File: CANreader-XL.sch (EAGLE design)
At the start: 100 parts, among them IC1 MCP2551, IC2 TJA1055T/3, IC3 BD9G101G, IC4 LM1117IMPX-3.3, IC6 STM32F107RBT, IC7 DP83848I, Q1 25MHz, SW1 SLEEP, SW2 TERM, U1 HC_05, X1 MINI-USB, X2 SWD, X3 GPIO, X4 UART, X5 CAN

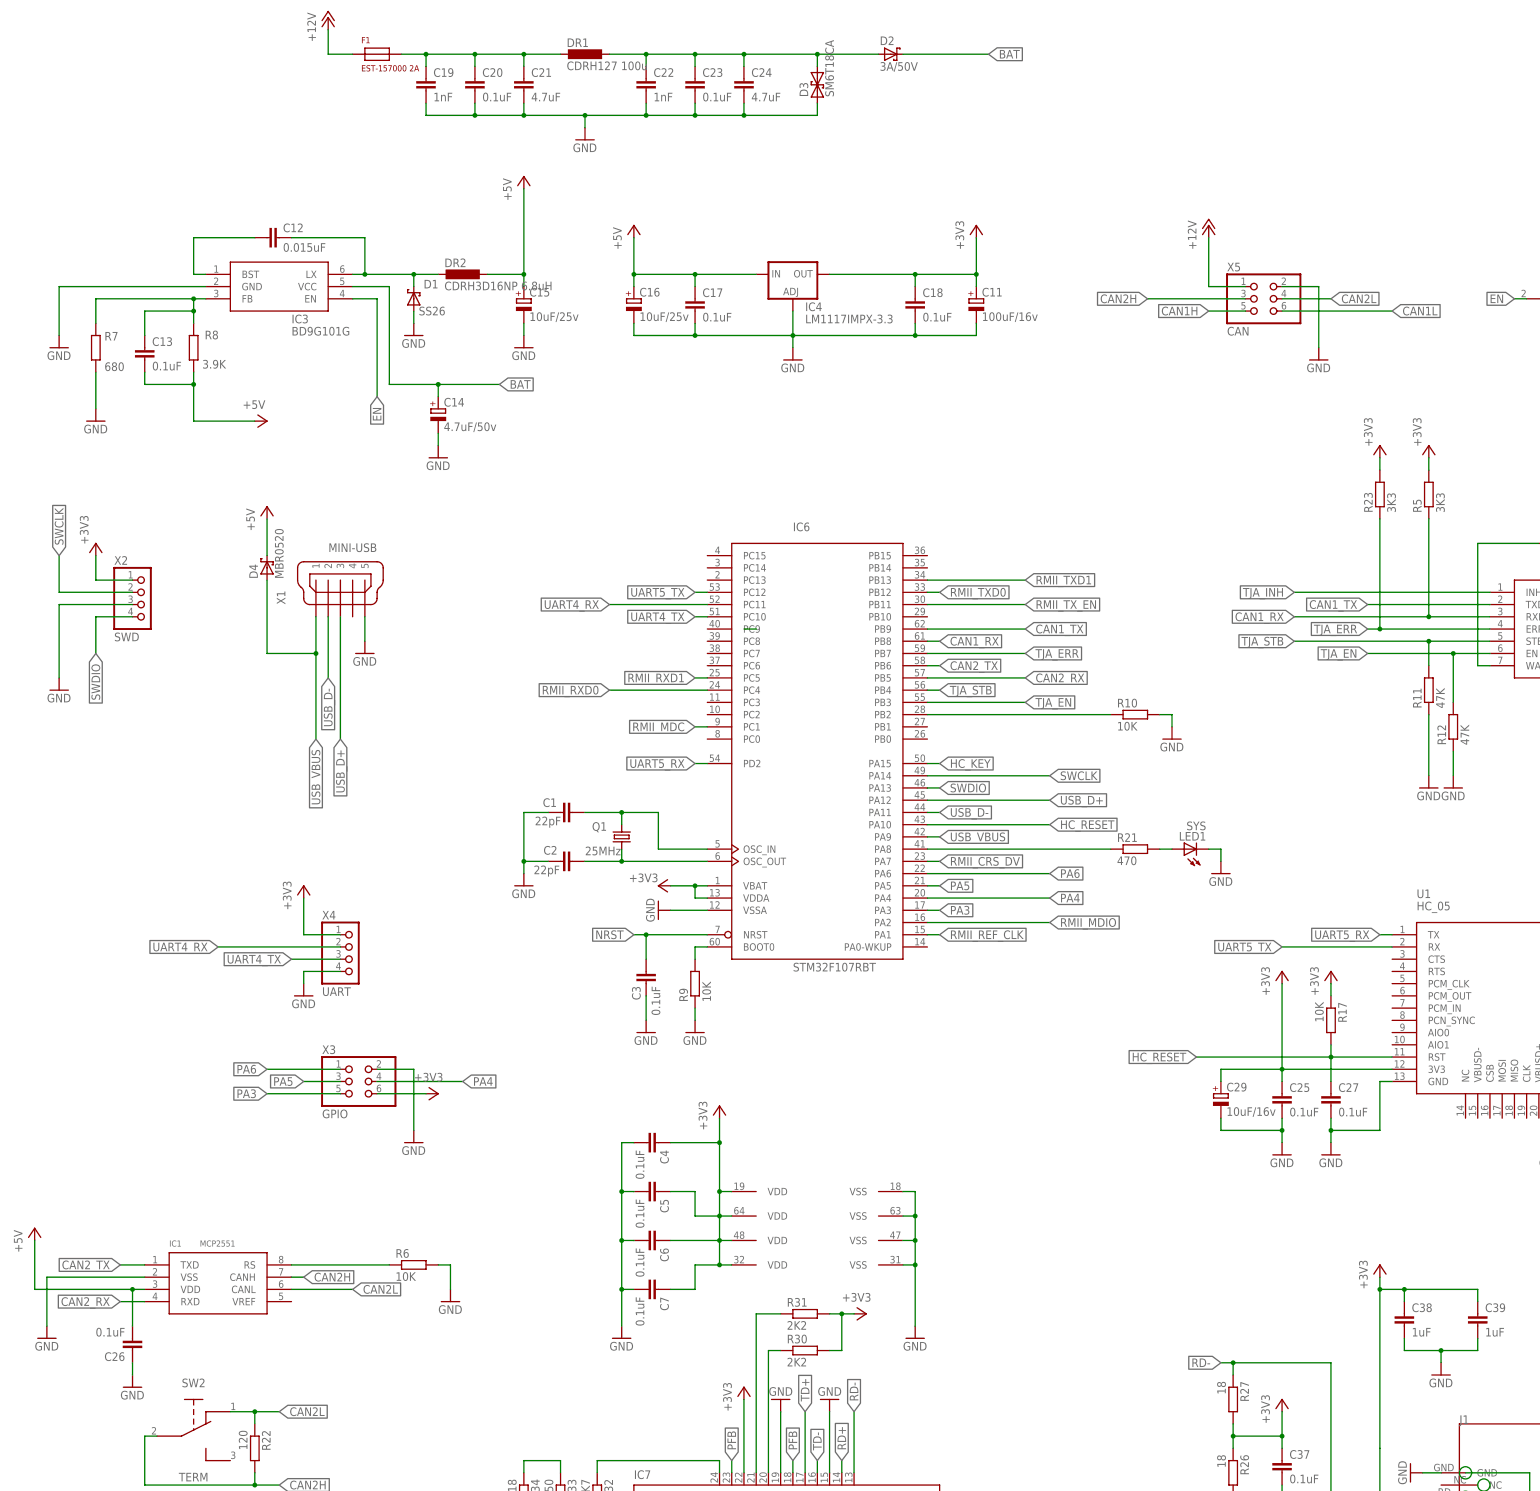
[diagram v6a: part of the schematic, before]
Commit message: MCP2562, usb connector
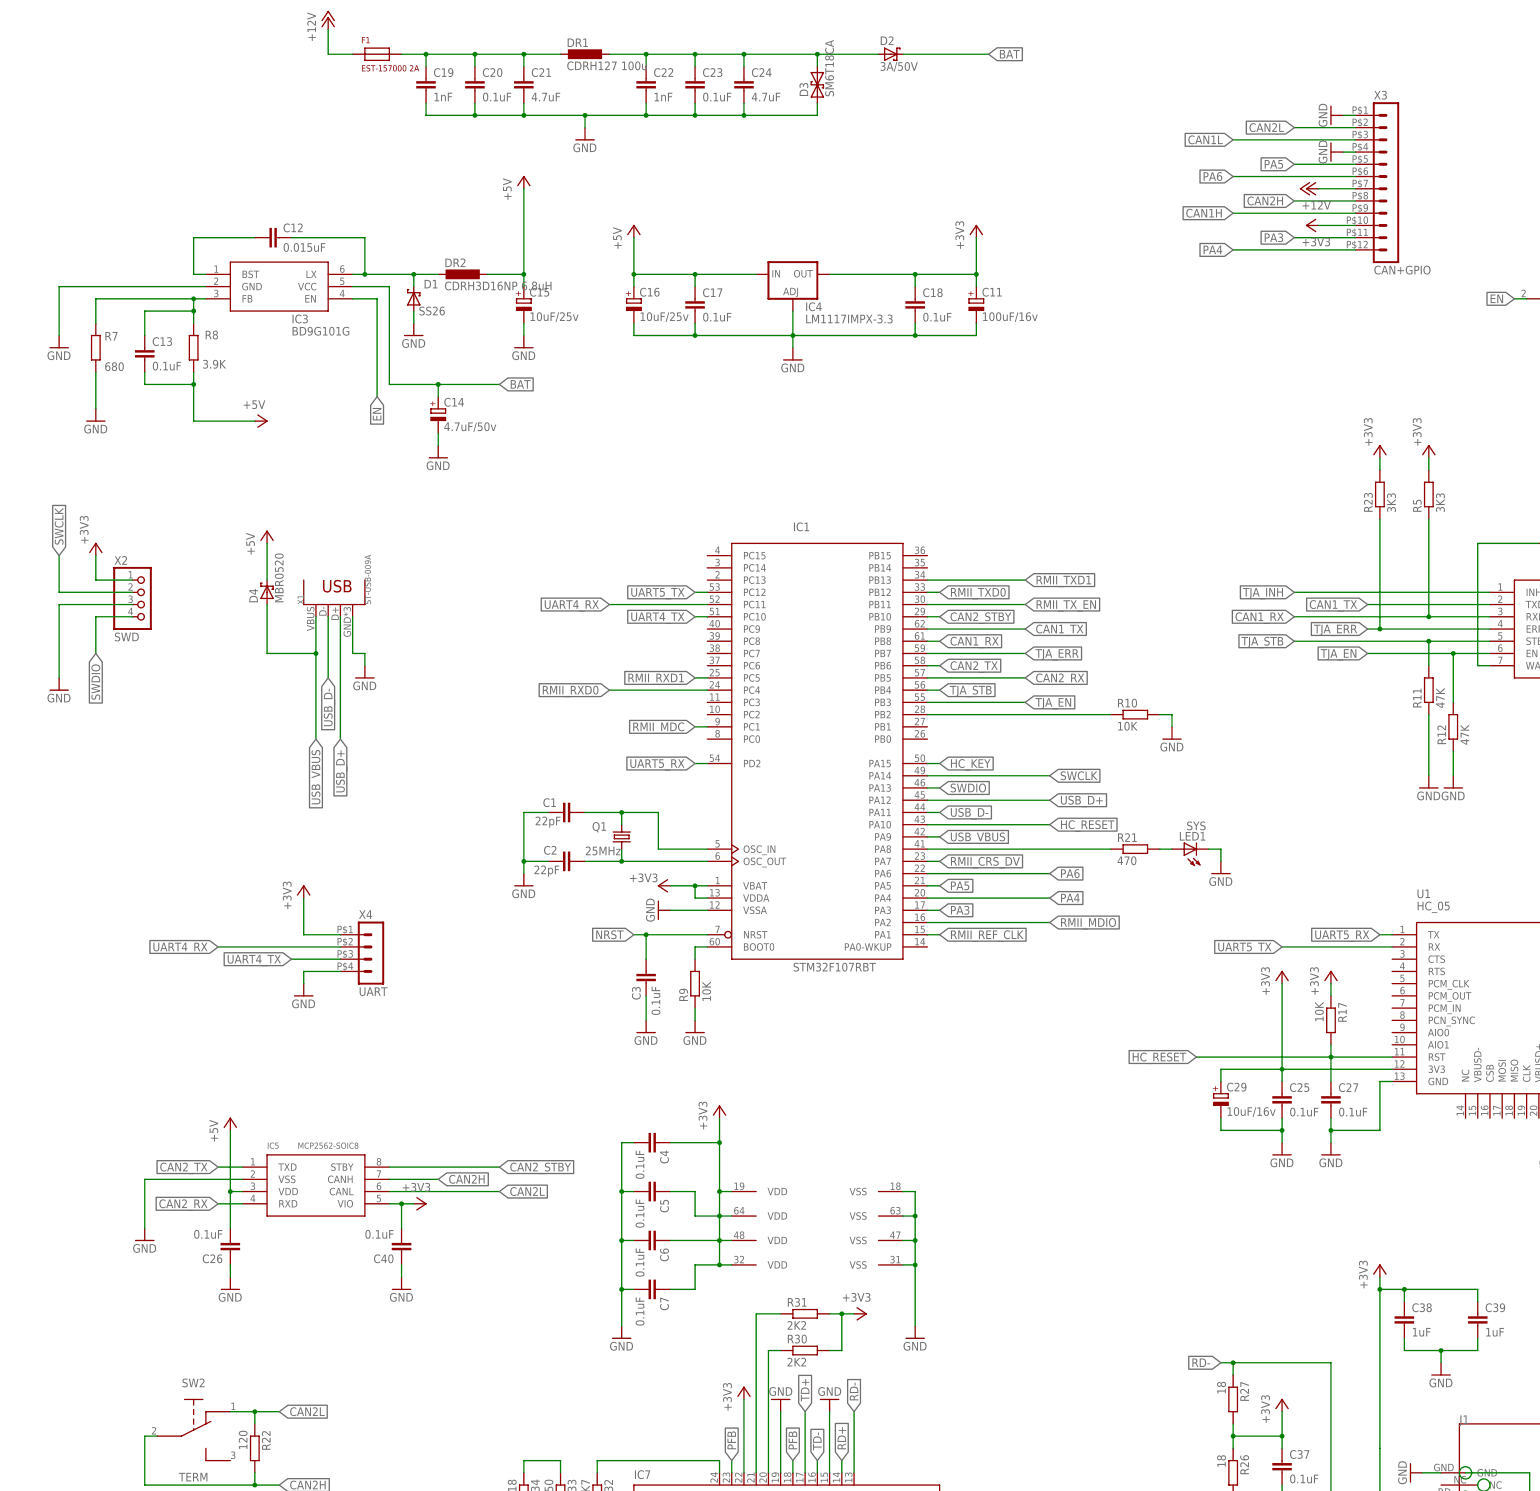
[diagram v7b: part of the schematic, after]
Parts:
- removed IC6: STM32F107RBT, micro-stm_v2:STM32F107RBT
- removed R6: 10K, rcl:R-EU_R0805
- removed X5: CAN, STM32_CAN-USB:PINHD-2X3/90
- added C40: 0.1uF, rcl:C-EUC0805
- added IC5: MCP2562-SOIC8, STM32_CAN-USB:MCP2562-SOIC8
- IC1: value MCP2551 -> STM32F107RBT; device STM32_CAN-USB:INTERFACE-MCP2551-I/SN(SOIC8) -> micro-stm_v2:STM32F107RBT
- X1: value MINI-USB -> ST-USB-009A; device STM32_CAN-USB:MINI-USB-UX60-MB-5ST -> Seeed-OPL-Connector:DIP-USB-B-TYPE-FMAL(4+2P-2.5-90D)
- X3: value GPIO -> CAN+GPIO; device STM32_CAN-USB:PINHD-2X3/90 -> con-molex-micro-fit-3_0:HEADER_POS12_43045-1200
- X4: device STM32_CAN-USB:PINHD-1X4/90 -> con-molex-micro-fit-3_0:HEADER_POS4_43045-0401
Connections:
- removed net N$5: IC1.RS, R6.1
- new net CAN2_STBY: IC1MCU.PB10, IC5.STBY
- net +12V: now also X3.7; no longer X5.1
- net +3V3: now also C40.2, IC1MCU.VBAT, IC1MCU.VDDA, IC1PWR.VDD@1, IC1PWR.VDD@2, IC1PWR.VDD@3, IC1PWR.VDD@4, IC5.VIO, X3.10; no longer IC6MCU.VBAT, IC6MCU.VDDA, IC6PWR.VDD@1, IC6PWR.VDD@2, IC6PWR.VDD@3, IC6PWR.VDD@4, X3.6
- net +5V: now also IC5.VDD; no longer IC1.VDD
- net CAN1H: now also X3.9; no longer X5.5
- net CAN1L: now also X3.3; no longer X5.6
- net CAN1_RX: now also IC1MCU.PB8; no longer IC6MCU.PB8
- net CAN1_TX: now also IC1MCU.PB9; no longer IC6MCU.PB9
- net CAN2H: now also IC5.CANH, X3.8; no longer IC1.CANH, X5.3
- net CAN2L: now also IC5.CANL, X3.2; no longer IC1.CANL, X5.4
- net CAN2_RX: now also IC1MCU.PB5, IC5.RXD; no longer IC1.RXD, IC6MCU.PB5
- net CAN2_TX: now also IC1MCU.PB6, IC5.TXD; no longer IC1.TXD, IC6MCU.PB6
- net GND: now also C40.1, IC1MCU.VSSA, IC1PWR.VSS@1, IC1PWR.VSS@2, IC1PWR.VSS@3, IC1PWR.VSS@4, IC5.VSS, X1.4, X3.1, X3.4; no longer IC1.VSS, IC6MCU.VSSA, IC6PWR.VSS@1, IC6PWR.VSS@2, IC6PWR.VSS@3, IC6PWR.VSS@4, R6.2, X1.5, X3.2, X5.2
- net HC_KEY: now also IC1MCU.PA15; no longer IC6MCU.PA15
- net HC_RESET: now also IC1MCU.PA10; no longer IC6MCU.PA10
- net N$1: now also IC1MCU.OSC_IN; no longer IC6MCU.OSC_IN
- net N$2: now also IC1MCU.OSC_OUT; no longer IC6MCU.OSC_OUT
- net N$3: now also IC1MCU.BOOT0; no longer IC6MCU.BOOT0
- net N$4: now also IC1MCU.PB2; no longer IC6MCU.PB2
- net N$6: now also IC1MCU.PA8; no longer IC6MCU.PA8
- net NRST: now also IC1MCU.NRST; no longer IC6MCU.NRST
- net PA3: now also IC1MCU.PA3, X3.11; no longer IC6MCU.PA3, X3.5
- net PA4: now also IC1MCU.PA4, X3.12; no longer IC6MCU.PA4, X3.4
- net PA5: now also IC1MCU.PA5, X3.5; no longer IC6MCU.PA5, X3.3
- net PA6: now also IC1MCU.PA6, X3.6; no longer IC6MCU.PA6, X3.1
- net RMII_CRS_DV: now also IC1MCU.PA7; no longer IC6MCU.PA7
- net RMII_MDC: now also IC1MCU.PC1; no longer IC6MCU.PC1
- net RMII_MDIO: now also IC1MCU.PA2; no longer IC6MCU.PA2
- net RMII_REF_CLK: now also IC1MCU.PA1; no longer IC6MCU.PA1
- net RMII_RXD0: now also IC1MCU.PC4; no longer IC6MCU.PC4
- net RMII_RXD1: now also IC1MCU.PC5; no longer IC6MCU.PC5
- net RMII_TXD0: now also IC1MCU.PB12; no longer IC6MCU.PB12
- net RMII_TXD1: now also IC1MCU.PB13; no longer IC6MCU.PB13
- net RMII_TX_EN: now also IC1MCU.PB11; no longer IC6MCU.PB11
- net SWCLK: now also IC1MCU.PA14; no longer IC6MCU.PA14
- net SWDIO: now also IC1MCU.PA13; no longer IC6MCU.PA13
- net TJA_EN: now also IC1MCU.PB3; no longer IC6MCU.PB3
- net TJA_ERR: now also IC1MCU.PB7; no longer IC6MCU.PB7
- net TJA_STB: now also IC1MCU.PB4; no longer IC6MCU.PB4
- net UART4_RX: now also IC1MCU.PC11; no longer IC6MCU.PC11
- net UART4_TX: now also IC1MCU.PC10; no longer IC6MCU.PC10
- net UART5_RX: now also IC1MCU.PD2; no longer IC6MCU.PD2
- net UART5_TX: now also IC1MCU.PC12; no longer IC6MCU.PC12
- net USB_D+: now also IC1MCU.PA12; no longer IC6MCU.PA12
- net USB_D-: now also IC1MCU.PA11; no longer IC6MCU.PA11
- net USB_VBUS: now also IC1MCU.PA9; no longer IC6MCU.PA9
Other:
- moved on the sheet: C26, D4

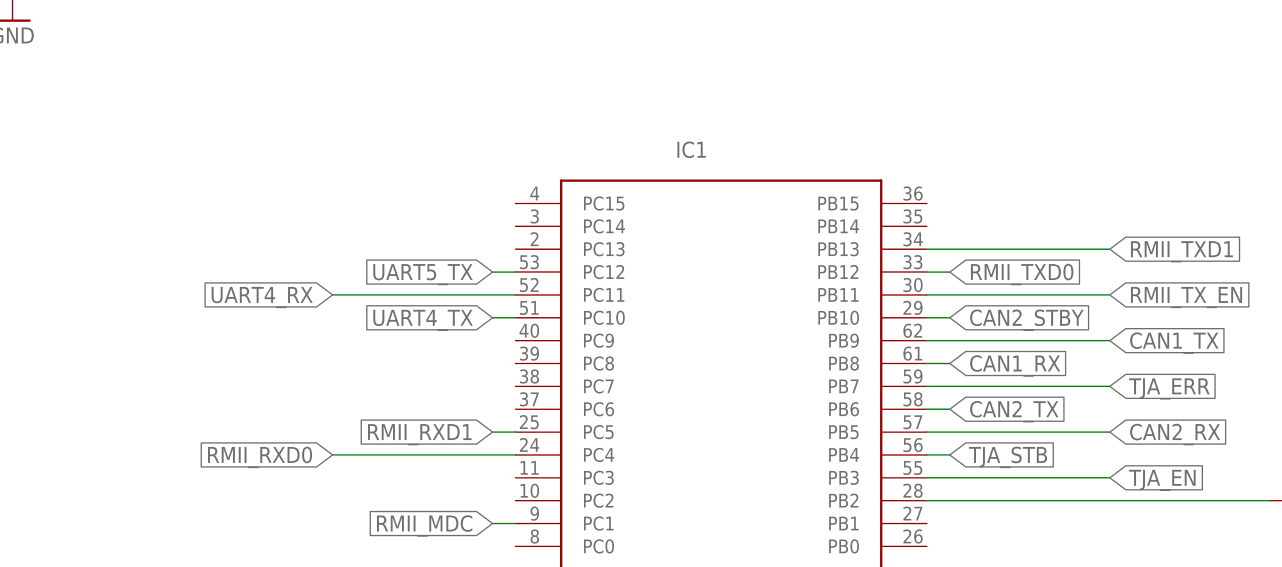
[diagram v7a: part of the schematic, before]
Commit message: CAN2_STBY, Heap size
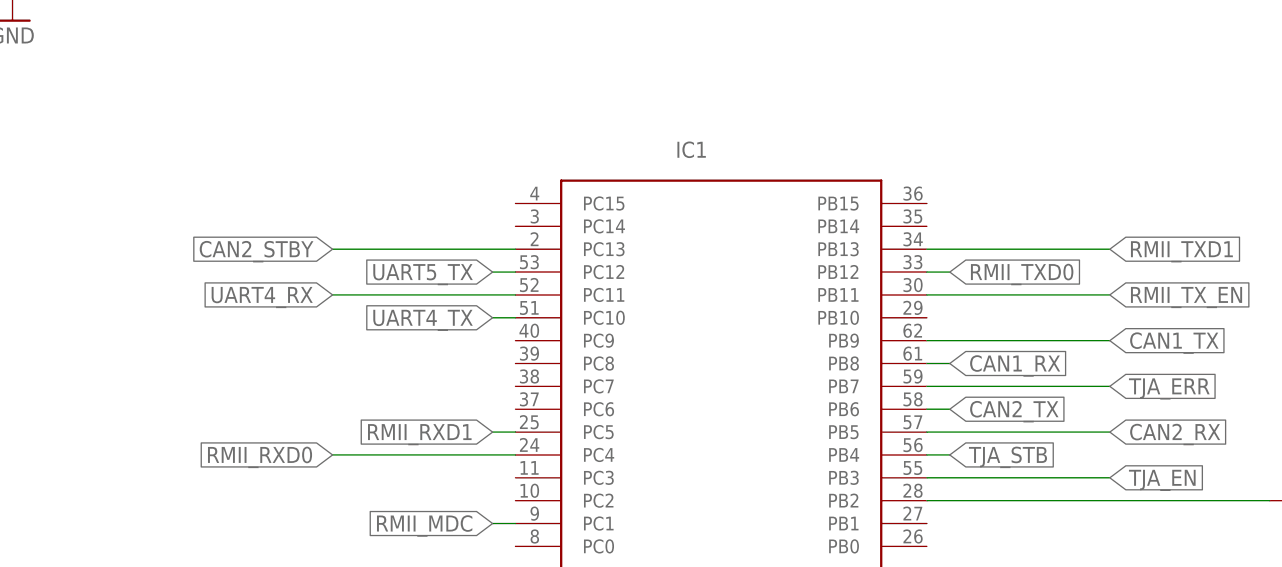
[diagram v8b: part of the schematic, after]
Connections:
- net CAN2_STBY: now also IC1MCU.PC13; no longer IC1MCU.PB10
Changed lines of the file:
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@@
 </segment>
 <segment>
-<pinref part="IC1" gate="MCU" pin="PB10"/>
-<wire x1="96.52" y1="66.04" x2="99.06" y2="66.04" width="0.1524" layer="91"/>
-<label x="99.06" y="66.04" size="1.778" layer="95" xref="yes"/>
+<label x="30.48" y="73.66" size="1.778" layer="95" rot="R180" xref="yes"/>
+<pinref part="IC1" gate="MCU" pin="PC13"/>
+<wire x1="30.48" y1="73.66" x2="50.8" y2="73.66" width="0.1524" layer="91"/>
 </segment>
 </net>
